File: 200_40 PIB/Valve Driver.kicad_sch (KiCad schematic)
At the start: 39 parts, among them J4 53398-0671, Q10 IRF7832, U1 LT3065EDDPBF, U2 MIC4424YM, U3 MIC4424YM, U6 LM1117MP-3.3, U8 74LVC1GU04DRL, U9 74LVC2G126DCU

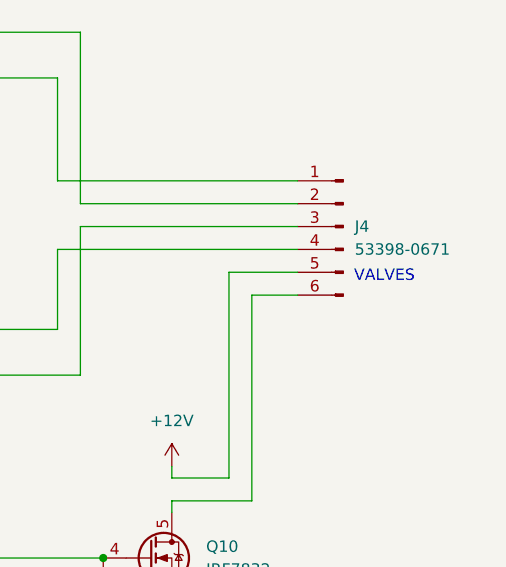
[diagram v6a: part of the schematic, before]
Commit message: fix DRC warnings, check DRC rules against JLC spec, replace all connector symbols with proper MP symbols (MP to ground), fix ground stitching
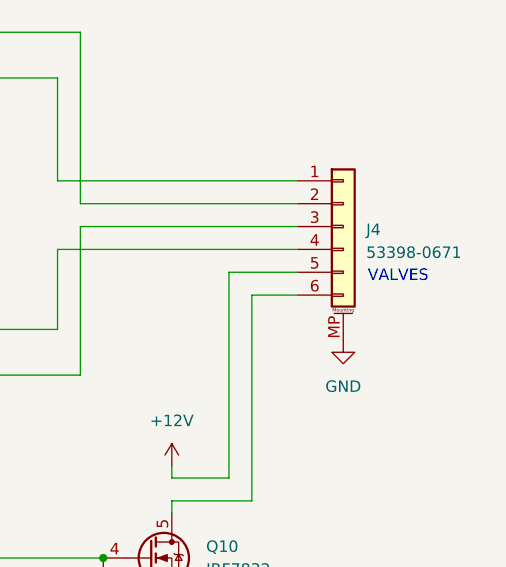
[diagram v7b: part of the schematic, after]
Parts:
- removed J4: 53398-0671, Connector_Molex:Molex_PicoBlade_53398-0671_1x06-1MP_P1.25mm_Vertical, symbol Connector:Conn_01x06_Pin
- added J4: 53398-0671, Connector_Molex:Molex_PicoBlade_53398-0671_1x06-1MP_P1.25mm_Vertical, symbol Connector_Generic_MountingPin:Conn_01x06_MountingPin
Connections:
- net +12V: now also J4.5 (Pin_5)
- net GND: now also J4.MP (MountPin)
- net at Q10.5 (D), Q10.6 (D), Q10.7 (D)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: now also J4.6 (Pin_6)
- net at U2.5 (OUTB): now also J4.1 (Pin_1)
- net at U2.7 (OUTA): now also J4.2 (Pin_2)
- net at U3.5 (OUTB): now also J4.3 (Pin_3)
- net at U3.7 (OUTA): now also J4.4 (Pin_4)
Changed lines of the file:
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@@
 	(text "VALVES"
 		(exclude_from_sim no)
-		(at 235.712 77.978 0)
+		(at 237.236 77.978 0)
 		(effects
 			(font
@@
 	(symbol
 		(lib_id "power:GND")
+		(at 231.14 85.09 0)
+		(unit 1)
+		(body_style 1)
+		(exclude_from_sim no)
+		(in_bom yes)
+		(on_board yes)
+		(in_pos_files yes)
+		(dnp no)
+		(fields_autoplaced yes)
+		(property "Reference" "#PWR0118"
+			(at 231.14 91.44 0)
+			(hide yes)
+			(show_name no)
+			(do_not_autoplace no)
+			(effects
+				(font
+					(size 1.27 1.27)
+				)
+			)
+		)
+		(property "Value" "GND"
+			(at 231.14 90.17 0)
+			(show_name no)
+			(do_not_autoplace no)
+			(effects
+				(font
+					(size 1.27 1.27)
+				)
+			)
+		)
+		(property "Footprint" ""
+			(at 231.14 85.09 0)
+			(hide yes)
+			(show_name no)
+			(do_not_autoplace no)
+			(effects
+				(font
+					(size 1.27 1.27)
+				)
+			)
+		)
+		(property "Datasheet" ""
+			(at 231.14 85.09 0)
+			(hide yes)
+			(show_name no)
+			(do_not_autoplace no)
+			(effects
+				(font
+					(size 1.27 1.27)
+				)
+			)
+		)
+		(property "Description" "Power symbol creates a global label with name \"GND\" , ground"
+			(at 231.14 85.09 0)
+			(hide yes)
+			(show_name no)
+			(do_not_autoplace no)
+			(effects
+				(font
+					(size 1.27 1.27)
+				)
+			)
+		)
+		(pin "1"
+		)
+		(instances
+			(project "PIB"
+				(path "/2bb2e4a1-de70-477a-a246-143db0a21e08/a3e2437a-f450-49da-ac0f-e1add7c59a42"
+					(reference "#PWR0118")
+					(unit 1)
+				)
+			)
+		)
+	)
+	(symbol
+		(lib_id "power:GND")
 		(at 45.72 142.24 0)
 		(unit 1)
@@
 	)
 	(symbol
-		(lib_id "Connector:Conn_01x06_Pin")
-		(at 231.14 72.39 0)
-		(mirror y)
-		(unit 1)
-		(body_style 1)
-		(exclude_from_sim no)
-		(in_bom yes)
-		(on_board yes)
-		(in_pos_files yes)
-		(dnp no)
-		(fields_autoplaced yes)
-		(property "Reference" "J4"
-			(at 232.41 72.3899 0)
-			(show_name no)
-			(do_not_autoplace no)
-			(effects
-				(font
-					(size 1.27 1.27)
-				)
-				(justify right)
-			)
-		)
-		(property "Value" "53398-0671"
-			(at 232.41 74.9299 0)
-			(show_name no)
-			(do_not_autoplace no)
-			(effects
-				(font
-					(size 1.27 1.27)
-				)
-				(justify right)
-			)
-		)
-		(property "Footprint" "Connector_Molex:Molex_PicoBlade_53398-0671_1x06-1MP_P1.25mm_Vertical"
-			(at 231.14 72.39 0)
-			(hide yes)
-			(show_name no)
-			(do_not_autoplace no)
-			(effects
-				(font
-					(size 1.27 1.27)
-				)
-			)
-		)
-		(property "Datasheet" ""
-			(at 231.14 72.39 0)
-			(hide yes)
-			(show_name no)
-			(do_not_autoplace no)
-			(effects
-				(font
-					(size 1.27 1.27)
-				)
-			)
-		)
-		(property "Description" "Generic connector, single row, 01x06, script generated"
-			(at 231.14 72.39 0)
-			(hide yes)
-			(show_name no)
-			(do_not_autoplace no)
-			(effects
-				(font
-					(size 1.27 1.27)
-				)
-			)
-		)
-		(pin "2"
-		)
-		(pin "3"
-		)
-		(pin "6"
-		)
-		(pin "5"
-		)
-		(pin "1"
-		)
-		(pin "4"
-		)
-		(instances
-			(project "PIB"
-				(path "/2bb2e4a1-de70-477a-a246-143db0a21e08/a3e2437a-f450-49da-ac0f-e1add7c59a42"
-					(reference "J4")
-					(unit 1)
-				)
-			)
-		)
-	)
-	(symbol
 		(lib_id "Device:R")
 		(at 152.4 62.23 0)
@@
 					(unit 1)
 				)
+			)
+		)
+	)
+	(symbol
+		(lib_id "Connector_Generic_MountingPin:Conn_01x06_MountingPin")
+		(at 231.14 72.39 0)
+		(unit 1)
+		(body_style 1)
+		(exclude_from_sim no)
+		(in_bom yes)
+		(on_board yes)
+		(in_pos_files yes)
+		(dnp no)
+		(fields_autoplaced yes)
+		(property "Reference" "J4"
+			(at 233.68 72.7455 0)
+			(show_name no)
+			(do_not_autoplace no)
+			(effects
+				(font
+					(size 1.27 1.27)
+				)
+				(justify left)
+			)
+		)
+		(property "Value" "53398-0671"
+			(at 233.68 75.2855 0)
+			(show_name no)
+			(do_not_autoplace no)
+			(effects
+				(font
+					(size 1.27 1.27)
+				)
+				(justify left)
+			)
+		)
+		(property "Footprint" "Connector_Molex:Molex_PicoBlade_53398-0671_1x06-1MP_P1.25mm_Vertical"
+			(at 231.14 72.39 0)
+			(hide yes)
+			(show_name no)
+			(do_not_autoplace no)
+			(effects
+				(font
+					(size 1.27 1.27)
+				)
+			)
+		)
+		(property "Datasheet" ""
+			(at 231.14 72.39 0)
+			(hide yes)
+			(show_name no)
+			(do_not_autoplace no)
+			(effects
+				(font
+					(size 1.27 1.27)
+				)
+			)
+		)
+		(property "Description" "Generic connectable mounting pin connector, single row, 01x06, script generated (kicad-library-utils/schlib/autogen/connector/)"
+			(at 231.14 72.39 0)
+			(hide yes)
+			(show_name no)
+			(do_not_autoplace no)
+			(effects
+				(font
+					(size 1.27 1.27)
+				)
+			)
+		)
+		(pin "6"
+		)
+		(pin "4"
+		)
+		(pin "2"
+		)
+		(pin "3"
+		)
+		(pin "MP"
+		)
+		(pin "1"
+		)
+		(pin "5"
+		)
+		(instances
+			(project "PIB"
+				(path "/2bb2e4a1-de70-477a-a246-143db0a21e08/a3e2437a-f450-49da-ac0f-e1add7c59a42"
+					(reference "J4")
+					(unit 1)
+				)

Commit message: add TVS diodes
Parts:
- added C68: 10uF, Capacitor_SMD:C_0805_2012Metric, symbol Device:C
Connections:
- net +12V: now also C68.1
- net GND: now also C68.2
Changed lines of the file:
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@@
 	)
 	(junction
+		(at 204.47 95.25)
+		(diameter 0)
+		(color 0 0 0 0)
+	)
+	(junction
 		(at 46.99 38.1)
 		(diameter 0)
@@
 	(wire
 		(pts
-			(xy 218.44 77.47) (xy 218.44 100.33)
+			(xy 218.44 77.47) (xy 218.44 95.25)
 		)
 		(stroke
@@
 	(wire
 		(pts
-			(xy 218.44 100.33) (xy 212.09 100.33)
+			(xy 218.44 95.25) (xy 204.47 95.25)
 		)
 		(stroke
@@
 	(wire
 		(pts
-			(xy 212.09 100.33) (xy 212.09 99.06)
-		)
-		(stroke
-			(width 0)
-			(type default)
-		)
-	)
-	(wire
-		(pts
 			(xy 80.01 22.86) (xy 88.9 22.86)
 		)
@@
 	)
 	(symbol
+		(lib_id "Device:C")
+		(at 204.47 99.06 0)
+		(unit 1)
+		(body_style 1)
+		(exclude_from_sim no)
+		(in_bom yes)
+		(on_board yes)
+		(in_pos_files yes)
+		(dnp no)
+		(property "Reference" "C68"
+			(at 207.01 97.79 0)
+			(show_name no)
+			(do_not_autoplace no)
+			(effects
+				(font
+					(size 1.27 1.27)
+				)
+				(justify left)
+			)
+		)
+		(property "Value" "10uF"
+			(at 207.01 100.33 0)
+			(show_name no)
+			(do_not_autoplace no)
+			(effects
+				(font
+					(size 1.27 1.27)
+				)
+				(justify left)
+			)
+		)
+		(property "Footprint" "Capacitor_SMD:C_0805_2012Metric"
+			(at 205.4352 102.87 0)
+			(hide yes)
+			(show_name no)
+			(do_not_autoplace no)
+			(effects
+				(font
+					(size 1.27 1.27)
+				)
+			)
+		)
+		(property "Datasheet" ""
+			(at 204.47 99.06 0)
+			(hide yes)
+			(show_name no)
+			(do_not_autoplace no)
+			(effects
+				(font
+					(size 1.27 1.27)
+				)
+			)
+		)
+		(property "Description" "Unpolarized capacitor"
+			(at 204.47 99.06 0)
+			(hide yes)
+			(show_name no)
+			(do_not_autoplace no)
+			(effects
+				(font
+					(size 1.27 1.27)
+				)
+			)
+		)
+		(pin "1"
+		)
+		(pin "2"
+		)
+		(instances
+			(project "PIB"
+				(path "/2bb2e4a1-de70-477a-a246-143db0a21e08/a3e2437a-f450-49da-ac0f-e1add7c59a42"
+					(reference "C68")
+					(unit 1)
+				)
+			)
+		)
+	)
+	(symbol
 		(lib_id "power:+12V")
 		(at 88.9 22.86 0)
@@
 	)
 	(symbol
+		(lib_id "power:GND")
+		(at 204.47 102.87 0)
+		(unit 1)
+		(body_style 1)
+		(exclude_from_sim no)
+		(in_bom yes)
+		(on_board yes)
+		(in_pos_files yes)
+		(dnp no)
+		(property "Reference" "#PWR0150"
+			(at 204.47 109.22 0)
+			(hide yes)
+			(show_name no)
+			(do_not_autoplace no)
+			(effects
+				(font
+					(size 1.27 1.27)
+				)
+			)
+		)
+		(property "Value" "GND"
+			(at 201.676 105.156 0)
+			(show_name no)
+			(do_not_autoplace no)
+			(effects
+				(font
+					(size 1.27 1.27)
+				)
+			)
+		)
+		(property "Footprint" ""
+			(at 204.47 102.87 0)
+			(hide yes)
+			(show_name no)
+			(do_not_autoplace no)
+			(effects
+				(font
+					(size 1.27 1.27)
+				)
+			)
+		)
+		(property "Datasheet" ""
+			(at 204.47 102.87 0)
+			(hide yes)
+			(show_name no)
+			(do_not_autoplace no)
+			(effects
+				(font
+					(size 1.27 1.27)
+				)
+			)
+		)
+		(property "Description" "Power symbol creates a global label with name \"GND\" , ground"
+			(at 204.47 102.87 0)
+			(hide yes)
+			(show_name no)
+			(do_not_autoplace no)
+			(effects
+				(font
+					(size 1.27 1.27)
+				)
+			)
+		)
+		(pin "1"
+		)
+		(instances
+			(project "PIB"
+				(path "/2bb2e4a1-de70-477a-a246-143db0a21e08/a3e2437a-f450-49da-ac0f-e1add7c59a42"
+					(reference "#PWR0150")
+					(unit 1)
+				)
+			)
+		)
+	)
+	(symbol
 		(lib_id "power:+12V")
 		(at 24.13 96.52 0)
@@
 	(symbol
 		(lib_id "power:+12V")
-		(at 212.09 99.06 0)
+		(at 204.47 95.25 0)
 		(unit 1)
 		(body_style 1)
@@
 		(fields_autoplaced yes)
 		(property "Reference" "#PWR06"
-			(at 212.09 102.87 0)
+			(at 204.47 99.06 0)
 			(hide yes)
 			(show_name no)
@@
 		)
 		(property "Value" "+12V"
-			(at 212.09 93.98 0)
+			(at 204.47 90.17 0)
 			(show_name no)
 			(do_not_autoplace no)
@@
 		)
 		(property "Footprint" ""
-			(at 212.09 99.06 0)
+			(at 204.47 95.25 0)
 			(hide yes)
 			(show_name no)
@@
 		)
 		(property "Datasheet" ""
-			(at 212.09 99.06 0)
+			(at 204.47 95.25 0)
 			(hide yes)
 			(show_name no)
@@
 		)
 		(property "Description" "Power symbol creates a global label with name \"+12V\""
-			(at 212.09 99.06 0)
+			(at 204.47 95.25 0)
 			(hide yes)
 			(show_name no)
